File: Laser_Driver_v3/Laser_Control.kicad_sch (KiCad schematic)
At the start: 15 parts, among them U30 74AHCT125, U31 AD9833xRM, U32 AD5064BRUZ, U33 AD9833xRM, U833 AD9833xRM (ref), U834 AD9833xRM (ref)

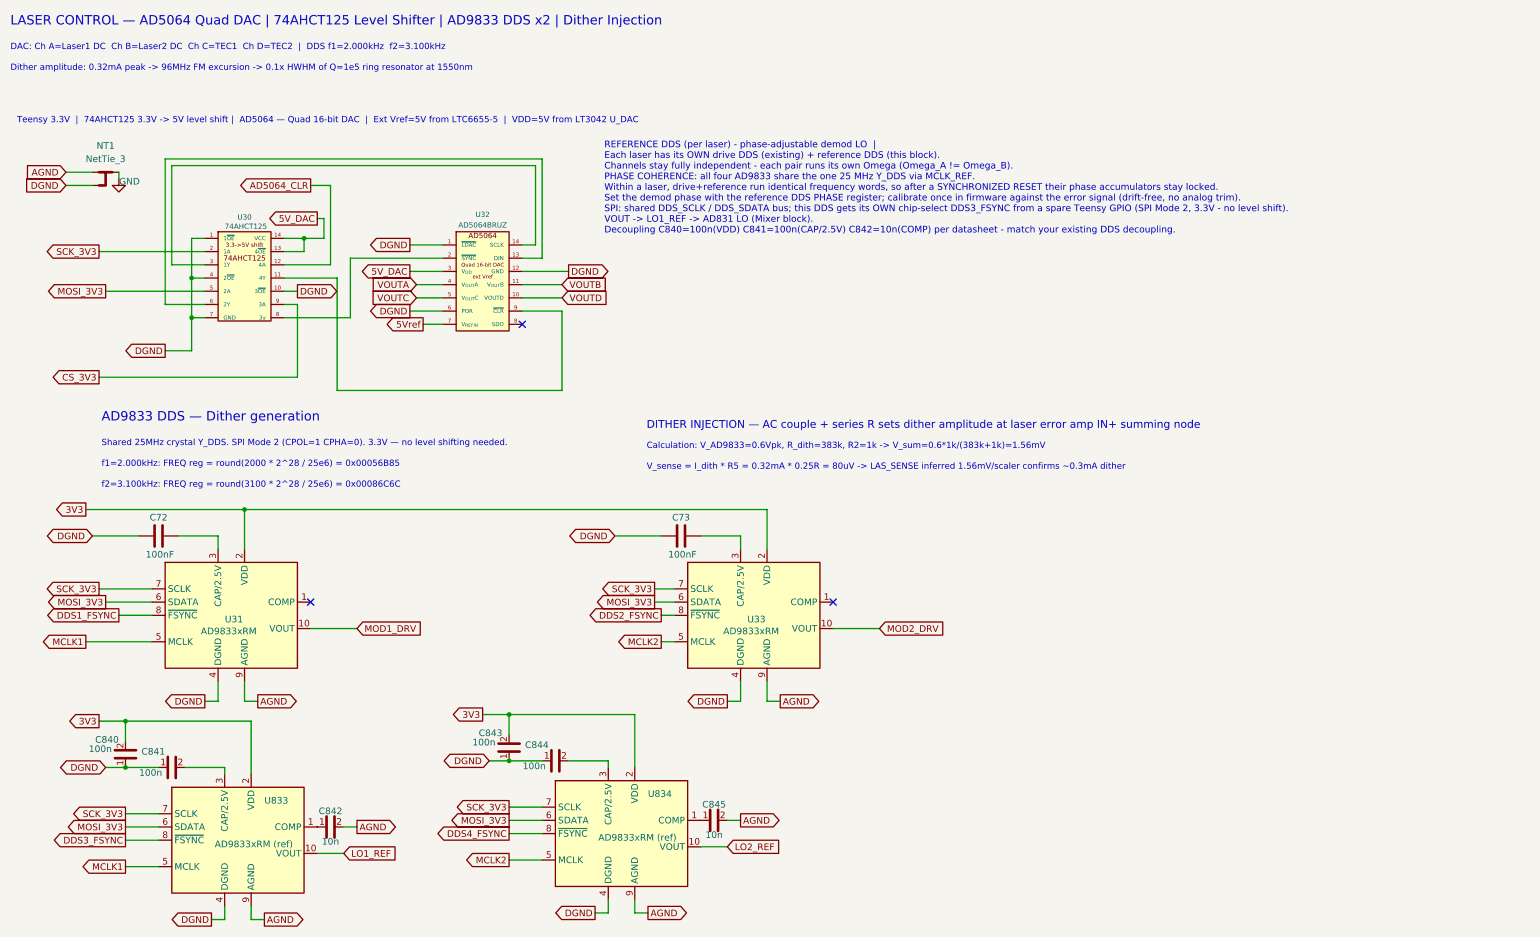
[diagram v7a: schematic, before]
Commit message: Updated the RF modulation implementation.
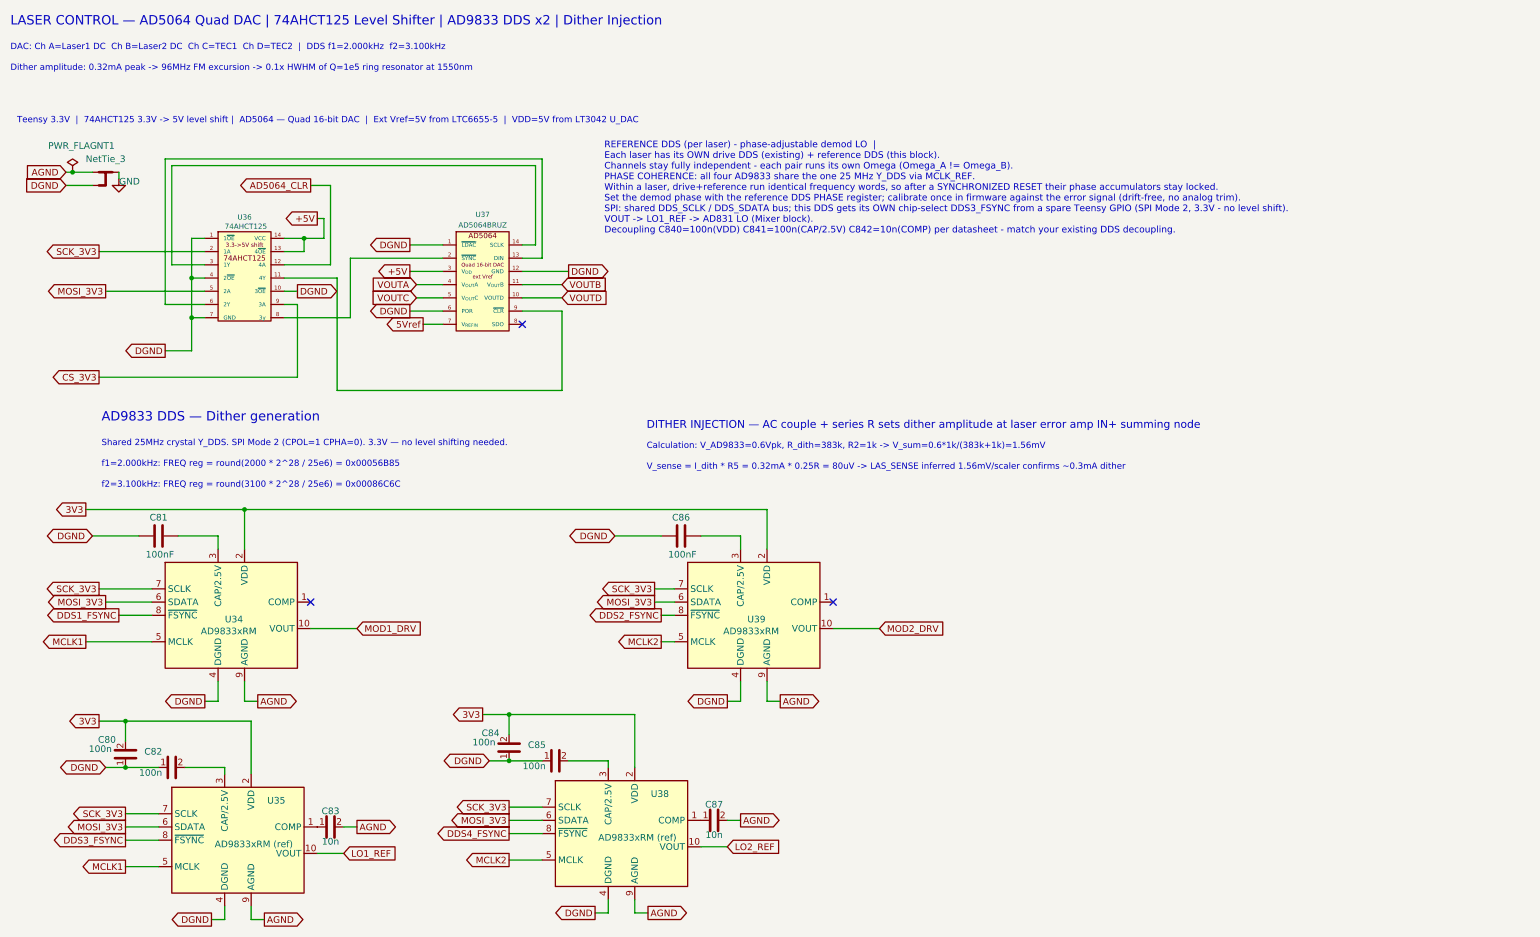
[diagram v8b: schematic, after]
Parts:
- renumbered C840 to C80, C72 to C81, C841 to C82, C842 to C83, C843 to C84, C844 to C85, C73 to C86, C845 to C87, U31 to U34, U833 to U35, U30 to U36, U32 to U37, U834 to U38, U33 to U39
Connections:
- net 5V_DAC renamed +5V
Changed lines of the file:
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@@
 	)
 	(junction
+		(at 25.4 44.45)
+		(diameter 0)
+		(color 0 0 0 0)
+	)
+	(junction
 		(at 35.56 158.75)
 		(diameter 0)
@@
 	(wire
 		(pts
-			(xy 24.13 44.45) (xy 29.21 44.45)
+			(xy 24.13 44.45) (xy 25.4 44.45)
 		)
 		(stroke
@@
 	(wire
 		(pts
+			(xy 25.4 44.45) (xy 29.21 44.45)
+		)
+		(stroke
+			(width 0)
+			(type default)
+		)
+	)
+	(wire
+		(pts
 			(xy 78.74 72.39) (xy 78.74 60.96)
 		)
@@
 		)
 	)
-	(global_label "5V_DAC"
+	(global_label "+5V"
 		(shape output)
 		(at 90.17 63.5 180)
@@
 		)
 		(property "Intersheetrefs" "${INTERSHEET_REFS}"
-			(at 80.2905 63.5 0)
+			(at 83.3143 63.5 0)
 			(hide yes)
 			(show_name no)
@@
 		)
 	)
-	(global_label "5V_DAC"
+	(global_label "+5V"
 		(shape output)
 		(at 72.39 53.34 180)
@@
 		)
 		(property "Intersheetrefs" "${INTERSHEET_REFS}"
-			(at 62.5105 53.34 0)
+			(at 65.5343 53.34 0)
 			(hide yes)
 			(show_name no)
@@
 		(in_pos_files yes)
 		(dnp no)
-		(property "Reference" "#PWR027"
+		(property "Reference" "#PWR025"
 			(at 34.29 52.07 0)
 			(hide yes)
@@
 			(project "laser_driver_v3"
 				(path "/b2c3d4e5-f6a7-8901-bcde-f12345678901/e4d7b089-62e9-414f-b4cc-abd1480c07cf"
-					(reference "#PWR027")
+					(reference "#PWR025")
 					(unit 1)
 				)
@@
 		(in_pos_files yes)
 		(dnp no)
-		(property "Reference" "C841"
+		(property "Reference" "C82"
 			(at 40.894 155.702 90)
 			(show_name no)
@@
 			(project "laser_driver_v3"
 				(path "/b2c3d4e5-f6a7-8901-bcde-f12345678901/e4d7b089-62e9-414f-b4cc-abd1480c07cf"
-					(reference "C841")
+					(reference "C82")
 					(unit 1)
 				)
@@
 		(in_pos_files yes)
 		(dnp no)
-		(property "Reference" "U833"
+		(property "Reference" "U35"
 			(at 64.516 165.1 0)
 			(show_name no)
@@
 			(project "laser_driver_v3"
 				(path "/b2c3d4e5-f6a7-8901-bcde-f12345678901/e4d7b089-62e9-414f-b4cc-abd1480c07cf"
-					(reference "U833")
+					(reference "U35")
 					(unit 1)
 				)
@@
 		(in_pos_files yes)
 		(dnp no)
-		(property "Reference" "U31"
+		(property "Reference" "U34"
 			(at 56.388 130.302 0)
 			(show_name no)
@@
 			(project "laser_driver_v3"
 				(path "/b2c3d4e5-f6a7-8901-bcde-f12345678901/e4d7b089-62e9-414f-b4cc-abd1480c07cf"
-					(reference "U31")
+					(reference "U34")
 					(unit 1)
 				)
@@
 		(in_pos_files yes)
 		(dnp no)
-		(property "Reference" "C845"
+		(property "Reference" "C87"
 			(at 148.59 165.862 90)
 			(show_name no)
@@
 			(project "laser_driver_v3"
 				(path "/b2c3d4e5-f6a7-8901-bcde-f12345678901/e4d7b089-62e9-414f-b4cc-abd1480c07cf"
-					(reference "C845")
+					(reference "C87")
 					(unit 1)
 				)
@@
 		(in_pos_files yes)
 		(dnp no)
-		(property "Reference" "U834"
+		(property "Reference" "U38"
 			(at 138.176 163.83 0)
 			(show_name no)
@@
 			(project "laser_driver_v3"
 				(path "/b2c3d4e5-f6a7-8901-bcde-f12345678901/e4d7b089-62e9-414f-b4cc-abd1480c07cf"
-					(reference "U834")
+					(reference "U38")
+					(unit 1)
+				)
+			)
+		)
+	)
+	(symbol
+		(lib_id "power:PWR_FLAG")
+		(at 25.4 44.45 0)
+		(unit 1)
+		(body_style 1)
+		(exclude_from_sim no)
+		(in_bom yes)
+		(on_board yes)
+		(in_pos_files yes)
+		(dnp no)
+		(fields_autoplaced yes)
+		(property "Reference" "#FLG06"
+			(at 25.4 42.545 0)
+			(hide yes)
+			(show_name no)
+			(do_not_autoplace no)
+			(effects
+				(font
+					(size 1.27 1.27)
+				)
+			)
+		)
+		(property "Value" "PWR_FLAG"
+			(at 25.4 39.37 0)
+			(show_name no)
+			(do_not_autoplace no)
+			(effects
+				(font
+					(size 1.27 1.27)
+				)
+			)
+		)
+		(property "Footprint" ""
+			(at 25.4 44.45 0)
+			(hide yes)
+			(show_name no)
+			(do_not_autoplace no)
+			(effects
+				(font
+					(size 1.27 1.27)
+				)
+			)
+		)
+		(property "Datasheet" ""
+			(at 25.4 44.45 0)
+			(hide yes)
+			(show_name no)
+			(do_not_autoplace no)
+			(effects
+				(font
+					(size 1.27 1.27)
+				)
+			)
+		)
+		(property "Description" "Special symbol for telling ERC where power comes from"
+			(at 25.4 44.45 0)
+			(hide yes)
+			(show_name no)
+			(do_not_autoplace no)
+			(effects
+				(font
+					(size 1.27 1.27)
+				)
+			)
+		)
+		(pin "1"
+		)
+		(instances
+			(project "laser_driver_v3"
+				(path "/b2c3d4e5-f6a7-8901-bcde-f12345678901/e4d7b089-62e9-414f-b4cc-abd1480c07cf"
+					(reference "#FLG06")
 					(unit 1)
 				)
@@
 		(in_pos_files yes)
 		(dnp no)
-		(property "Reference" "U32"
+		(property "Reference" "U37"
 			(at 104.14 52.578 0)
 			(show_name no)
@@
 			(project "laser_driver_v3"
 				(path "/b2c3d4e5-f6a7-8901-bcde-f12345678901/e4d7b089-62e9-414f-b4cc-abd1480c07cf"
-					(reference "U32")
+					(reference "U37")
 					(unit 1)
 				)
@@
 		(in_pos_files yes)
 		(dnp no)
-		(property "Reference" "C842"
+		(property "Reference" "C83"
 			(at 74.93 167.132 90)
 			(show_name no)
@@
 			(project "laser_driver_v3"
 				(path "/b2c3d4e5-f6a7-8901-bcde-f12345678901/e4d7b089-62e9-414f-b4cc-abd1480c07cf"
-					(reference "C842")
+					(reference "C83")
 					(unit 1)
 				)
@@
 		(in_pos_files yes)
 		(dnp no)
-		(property "Reference" "C73"
+		(property "Reference" "C86"
 			(at 142.24 110.744 90)
 			(show_name no)
@@
 			(project "laser_driver_v3"
 				(path "/b2c3d4e5-f6a7-8901-bcde-f12345678901/e4d7b089-62e9-414f-b4cc-abd1480c07cf"
-					(reference "C73")
+					(reference "C86")
 					(unit 1)
 				)
@@
 		(in_pos_files yes)
 		(dnp no)
-		(property "Reference" "U30"
+		(property "Reference" "U36"
 			(at 58.42 53.086 0)
 			(show_name no)
@@
 			(project "laser_driver_v3"
 				(path "/b2c3d4e5-f6a7-8901-bcde-f12345678901/e4d7b089-62e9-414f-b4cc-abd1480c07cf"
-					(reference "U30")
+					(reference "U36")
 					(unit 1)
 				)
@@
 		(in_pos_files yes)
 		(dnp no)
-		(property "Reference" "C843"
+		(property "Reference" "C84"
 			(at 105.664 152.146 0)
 			(show_name no)
@@
 			(project "laser_driver_v3"
 				(path "/b2c3d4e5-f6a7-8901-bcde-f12345678901/e4d7b089-62e9-414f-b4cc-abd1480c07cf"
-					(reference "C843")
+					(reference "C84")
 					(unit 1)
 				)
@@
 		(in_pos_files yes)
 		(dnp no)
-		(property "Reference" "C844"
+		(property "Reference" "C85"
 			(at 114.554 154.432 90)
 			(show_name no)
@@
 			(project "laser_driver_v3"
 				(path "/b2c3d4e5-f6a7-8901-bcde-f12345678901/e4d7b089-62e9-414f-b4cc-abd1480c07cf"
-					(reference "C844")
+					(reference "C85")
 					(unit 1)
 				)
@@
 		(in_pos_files yes)
 		(dnp no)
-		(property "Reference" "C72"
+		(property "Reference" "C81"
 			(at 41.91 110.744 90)
 			(show_name no)
@@
 			(project "laser_driver_v3"
 				(path "/b2c3d4e5-f6a7-8901-bcde-f12345678901/e4d7b089-62e9-414f-b4cc-abd1480c07cf"
-					(reference "C72")
+					(reference "C81")
 					(unit 1)
 				)
@@
 		(in_pos_files yes)
 		(dnp no)
-		(property "Reference" "C840"
+		(property "Reference" "C80"
 			(at 32.004 153.416 0)
 			(show_name no)
@@
 			(project "laser_driver_v3"
 				(path "/b2c3d4e5-f6a7-8901-bcde-f12345678901/e4d7b089-62e9-414f-b4cc-abd1480c07cf"
-					(reference "C840")
+					(reference "C80")
 					(unit 1)
 				)
@@
 		(in_pos_files yes)
 		(dnp no)
-		(property "Reference" "U33"
+		(property "Reference" "U39"
 			(at 156.718 130.302 0)
 			(show_name no)
@@
 			(project "laser_driver_v3"
 				(path "/b2c3d4e5-f6a7-8901-bcde-f12345678901/e4d7b089-62e9-414f-b4cc-abd1480c07cf"
-					(reference "U33")
+					(reference "U39")
 					(unit 1)
 				)
